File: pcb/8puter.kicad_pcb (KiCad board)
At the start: 2 copper layers, 120 x 100 mm, 82 parts, among them J1 PWR-DC, U2 74AHC74, U3 SN74LVC1G14DBV, U6 MAX811MEUS-T, X1 ECS-2200BX-100, Y1 1.8432MHz

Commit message: Gerber Plots
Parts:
- moved JTAG1 0.20 mm to (184.4, 119.4)
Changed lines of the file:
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@@
   )
   (footprint "Connector_PinHeader_2.00mm:PinHeader_1x05_P2.00mm_Vertical" (layer "F.Cu")
-    (at 184.598 119.445 180)
+    (at 184.398 119.445 180)
     (descr "Through hole straight pin header, 1x05, 2.00mm pitch, single row")
     (tags "Through hole pin header THT 1x05 2.00mm single row")
@@
     (style (thickness 0.1) (arrow_length 1.27) (text_position_mode 0) (extension_height 0.58642) (extension_offset 0.5) keep_text_aligned)
   )
-  (segment (start 186.198 110.545) (end 186.198 112.645) (width 0.2) (layer "F.Cu") (net 1))
   (segment (start 167.898 58.395) (end 167.898 59.597162) (width 0.2) (layer "F.Cu") (net 1))
   (segment (start 105.398 52.245) (end 102.798 52.245) (width 0.5) (layer "F.Cu") (net 1))
   (segment (start 167.798489 60.193327) (end 168.150162 60.545) (width 0.2) (layer "F.Cu") (net 1))
-  (segment (start 185.398 113.445) (end 184.598 113.445) (width 0.2) (layer "F.Cu") (net 1))
   (segment (start 132.298 38.645) (end 125.498 38.645) (width 0.4) (layer "F.Cu") (net 1))
   (segment (start 101.298 53.745) (end 96.198 53.745) (width 0.5) (layer "F.Cu") (net 1))
   (segment (start 169.8105 51.9825) (end 172.49752 51.9825) (width 0.2) (layer "F.Cu") (net 1))
   (segment (start 164.543349 51.9825) (end 169.8105 51.9825) (width 0.2) (layer "F.Cu") (net 1))
+  (segment (start 184.673 109.02) (end 186.198 110.545) (width 0.2) (layer "F.Cu") (net 1))
   (segment (start 167.898 58.395) (end 167.898 55.245) (width 0.2) (layer "F.Cu") (net 1))
   (segment (start 98.063 70.53) (end 103.683 70.53) (width 0.4) (layer "F.Cu") (net 1))
@@
   (segment (start 193.023 54.995) (end 193.023 58.82) (width 0.3) (layer "F.Cu") (net 1))
   (segment (start 188.473 58.52) (end 189.098 59.145) (width 0.3) (layer "F.Cu") (net 1))
-  (segment (start 186.198 112.645) (end 185.398 113.445) (width 0.2) (layer "F.Cu") (net 1))
+  (segment (start 184.673 108.645) (end 184.673 109.02) (width 0.2) (layer "F.Cu") (net 1))
   (segment (start 191.073 54.995) (end 191.073 53.82) (width 0.3) (layer "F.Cu") (net 1))
   (segment (start 188.473 54.995) (end 188.473 58.52) (width 0.3) (layer "F.Cu") (net 1))
@@
   (segment (start 172.49752 51.94548) (end 172.898 51.545) (width 0.2) (layer "F.Cu") (net 1))
   (segment (start 102.798 52.245) (end 102.698 52.345) (width 0.5) (layer "F.Cu") (net 1))
+  (segment (start 186.198 112.645) (end 185.398 113.445) (width 0.2) (layer "F.Cu") (net 1))
   (segment (start 167.898 59.597162) (end 167.798489 59.696673) (width 0.2) (layer "F.Cu") (net 1))
   (segment (start 189.198 59.245) (end 190.348 59.245) (width 0.2) (layer "F.Cu") (net 1))
@@
   (segment (start 106.398 70.545) (end 103.798 70.545) (width 0.4) (layer "F.Cu") (net 1))
   (segment (start 103.798 70.545) (end 103.748 70.595) (width 0.4) (layer "F.Cu") (net 1))
+  (segment (start 186.198 110.545) (end 186.198 112.645) (width 0.2) (layer "F.Cu") (net 1))
   (segment (start 141.998 46.845) (end 142.498 46.345) (width 0.4) (layer "F.Cu") (net 1))
   (segment (start 178.848005 112.307488) (end 178.848005 113.994988) (width 0.2) (layer "F.Cu") (net 1))
-  (segment (start 184.673 109.02) (end 186.198 110.545) (width 0.2) (layer "F.Cu") (net 1))
   (segment (start 167.898 55.245) (end 167.6355 54.9825) (width 0.2) (layer "F.Cu") (net 1))
   (segment (start 141.648 46.845) (end 141.998 46.845) (width 0.4) (layer "F.Cu") (net 1))
@@
   (segment (start 167.798489 59.696673) (end 167.798489 60.193327) (width 0.2) (layer "F.Cu") (net 1))
   (segment (start 103.683 70.53) (end 103.748 70.595) (width 0.4) (layer "F.Cu") (net 1))
-  (segment (start 184.673 108.645) (end 184.673 109.02) (width 0.2) (layer "F.Cu") (net 1))
+  (segment (start 185.398 113.445) (end 184.398 113.445) (width 0.2) (layer "F.Cu") (net 1))
   (via (at 202.898 126.345) (size 0.8) (drill 0.4) (layers "F.Cu" "B.Cu") (net 1))
   (via (at 202.898 124.145) (size 0.8) (drill 0.4) (layers "F.Cu" "B.Cu") (net 1))
@@
   (segment (start 202.898 124.145) (end 197.698 124.145) (width 0.4) (layer "B.Cu") (net 1))
   (segment (start 176.898005 113.944988) (end 179.298005 113.944988) (width 0.4) (layer "B.Cu") (net 1))
-  (segment (start 179.298005 113.944988) (end 184.098012 113.944988) (width 0.4) (layer "B.Cu") (net 1))
   (segment (start 183.028 44.715) (end 196.168 44.715) (width 0.5) (layer "B.Cu") (net 1))
   (segment (start 172.898 52.845) (end 175.098 55.045) (width 0.2) (layer "B.Cu") (net 1))
@@
   (segment (start 136.698 52.945) (end 136.198 53.445) (width 0.25) (layer "B.Cu") (net 1))
   (segment (start 185.598 78.945) (end 191.298 78.945) (width 0.5) (layer "B.Cu") (net 1))
-  (segment (start 184.098012 113.944988) (end 184.598 113.445) (width 0.4) (layer "B.Cu") (net 1))
+  (segment (start 179.298005 113.944988) (end 183.898012 113.944988) (width 0.4) (layer "B.Cu") (net 1))
   (segment (start 172.898 51.545) (end 172.898 52.845) (width 0.2) (layer "B.Cu") (net 1))
   (segment (start 125.598 38.645) (end 125.598 41.345) (width 0.4) (layer "B.Cu") (net 1))
@@
   (segment (start 141.498 41.2945) (end 141.498 38.945) (width 0.4) (layer "B.Cu") (net 1))
   (segment (start 198.198 85.845) (end 198.198 86.345) (width 0.5) (layer "B.Cu") (net 1))
+  (segment (start 183.898012 113.944988) (end 184.398 113.445) (width 0.4) (layer "B.Cu") (net 1))
   (segment (start 130.298 53.445) (end 128.008 51.155) (width 0.25) (layer "B.Cu") (net 1))
   (segment (start 115.598 46.245) (end 118.298 46.245) (width 0.4) (layer "B.Cu") (net 1))
@@
   (segment (start 182.398 130.245) (end 182.373989 130.269011) (width 0.2) (layer "B.Cu") (net 58))
   (segment (start 97.422011 130.269011) (end 95.498 128.345) (width 0.2) (layer "B.Cu") (net 58))
+  (segment (start 179.852219 111.890781) (end 180.298 111.445) (width 0.25) (layer "F.Cu") (net 59))
   (segment (start 179.852219 112.303274) (end 179.852219 111.890781) (width 0.25) (layer "F.Cu") (net 59))
   (segment (start 180.298 111.445) (end 184.598 111.445) (width 0.25) (layer "F.Cu") (net 59))
-  (segment (start 179.852219 111.890781) (end 180.298 111.445) (width 0.25) (layer "F.Cu") (net 59))
   (segment (start 186.198005 71.894988) (end 186.198005 66.945005) (width 0.15) (layer "F.Cu") (net 60))
   (segment (start 186.198 66.345) (end 186.523 66.02) (width 0.15) (layer "F.Cu") (net 60))
@@
   (segment (start 181.398 120.6575) (end 181.3105 120.745) (width 0.2) (layer "F.Cu") (net 74))
   (segment (start 180.539719 115.990774) (end 181.243774 115.990774) (width 0.2) (layer "F.Cu") (net 74))
-  (segment (start 180.539719 114.490774) (end 181.332365 114.490774) (width 0.15) (layer "F.Cu") (net 75))
-  (segment (start 183.098 117.945) (end 184.598 119.445) (width 0.15) (layer "F.Cu") (net 75))
-  (segment (start 183.098 116.256409) (end 183.098 117.945) (width 0.15) (layer "F.Cu") (net 75))
+  (segment (start 183.098 116.256409) (end 183.098 118.145) (width 0.15) (layer "F.Cu") (net 75))
   (segment (start 181.332365 114.490774) (end 183.098 116.256409) (width 0.15) (layer "F.Cu") (net 75))
-  (segment (start 186.898 115.145) (end 184.598 117.445) (width 0.2) (layer "F.Cu") (net 76))
-  (segment (start 186.898 109.045) (end 186.898 115.145) (width 0.2) (layer "F.Cu") (net 76))
-  (segment (start 184.598 117.195) (end 184.598 117.445) (width 0.15) (layer "F.Cu") (net 76))
-  (segment (start 181.393774 113.990774) (end 184.598 117.195) (width 0.15) (layer "F.Cu") (net 76))
-  (segment (start 180.539719 113.990774) (end 181.393774 113.990774) (width 0.15) (layer "F.Cu") (net 76))
+  (segment (start 183.098 118.145) (end 184.398 119.445) (width 0.15) (layer "F.Cu") (net 75))
+  (segment (start 180.539719 114.490774) (end 181.332365 114.490774) (width 0.15) (layer "F.Cu") (net 75))
   (segment (start 186.498 108.645) (end 186.898 109.045) (width 0.2) (layer "F.Cu") (net 76))
-  (segment (start 183.198 114.045) (end 184.598 115.445) (width 0.25) (layer "F.Cu") (net 77))
-  (segment (start 183.198 112.445) (end 183.198 114.045) (width 0.25) (layer "F.Cu") (net 77))
-  (segment (start 182.798 112.045) (end 183.198 112.445) (width 0.25) (layer "F.Cu") (net 77))
+  (segment (start 180.539719 113.990774) (end 181.32666 113.990774) (width 0.15) (layer "F.Cu") (net 76))
+  (segment (start 186.898 114.945) (end 184.398 117.445) (width 0.2) (layer "F.Cu") (net 76))
+  (segment (start 181.32666 113.990774) (end 183.44752 116.111634) (width 0.15) (layer "F.Cu") (net 76))
+  (segment (start 183.698 117.445) (end 184.398 117.445) (width 0.15) (layer "F.Cu") (net 76))
+  (segment (start 186.898 109.045) (end 186.898 114.945) (width 0.2) (layer "F.Cu") (net 76))
+  (segment (start 183.44752 116.111634) (end 183.44752 117.19452) (width 0.15) (layer "F.Cu") (net 76))
+  (segment (start 183.44752 117.19452) (end 183.698 117.445) (width 0.15) (layer "F.Cu") (net 76))
   (segment (start 180.539719 112.303281) (end 180.798 112.045) (width 0.25) (layer "F.Cu") (net 77))
+  (segment (start 182.798 112.045) (end 183.198 112.445) (width 0.25) (layer "F.Cu") (net 77))
   (segment (start 180.539719 112.990774) (end 180.539719 112.303281) (width 0.25) (layer "F.Cu") (net 77))
+  (segment (start 183.198 112.445) (end 183.198 114.245) (width 0.25) (layer "F.Cu") (net 77))
   (segment (start 180.798 112.045) (end 182.798 112.045) (width 0.25) (layer "F.Cu") (net 77))
+  (segment (start 183.198 114.245) (end 184.398 115.445) (width 0.25) (layer "F.Cu") (net 77))
   (segment (start 143.198 51.245) (end 143.198 53.3075) (width 0.25) (layer "F.Cu") (net 89))
   (segment (start 143.198 53.3075) (end 143.1605 53.345) (width 0.25) (layer "F.Cu") (net 89))

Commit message: board improvements
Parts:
- moved D1 0.05 mm to (100.3, 51.4), turned to -90 degrees
- turned U3 to -90 degrees
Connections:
- CS_SEL1 pad 5: GND -> unconnected-(CS_SEL1-Pad5)
- DEBUG1 pad 30: RDY -> ~{IRQ}
- DEBUG1 pad 32: CLOCK -> RDY
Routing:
- net ~{IRQ}: track 70.3 -> 190.2 mm
- net CLOCK: track 276.9 -> 157.8 mm
- net +5V: track 250.0 -> 187.8 mm, vias 5 -> 6
- net GND: track 253.9 -> 225.0 mm, vias 28 -> 26
- net ADDR0: track 178.5 -> 168.7 mm
- net ADDR1: track 184.7 -> 176.3 mm
- net RDY: track 189.7 -> 185.4 mm
- net Net-(C18-Pad1): track 7.55 -> 10.9 mm
- net Net-(U2-Pad12): track 7.45 -> 9.47 mm
- net Net-(U2-Pad11): track 8.96 -> 7.68 mm
- net Net-(C13-Pad1): track 52.2 -> 53.4 mm
- net Net-(SERC1-Pad4): track 25.3 -> 24.2 mm
- net /Peripheral Handler/PC1: track 53.1 -> 53.9 mm
- net /Power/PWR: track 23.4 -> 24.0 mm
- net Net-(D1-Pad1): track 3.16 -> 2.60 mm
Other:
- board text added: "~{IRQ}"
- board text removed: "CLK"

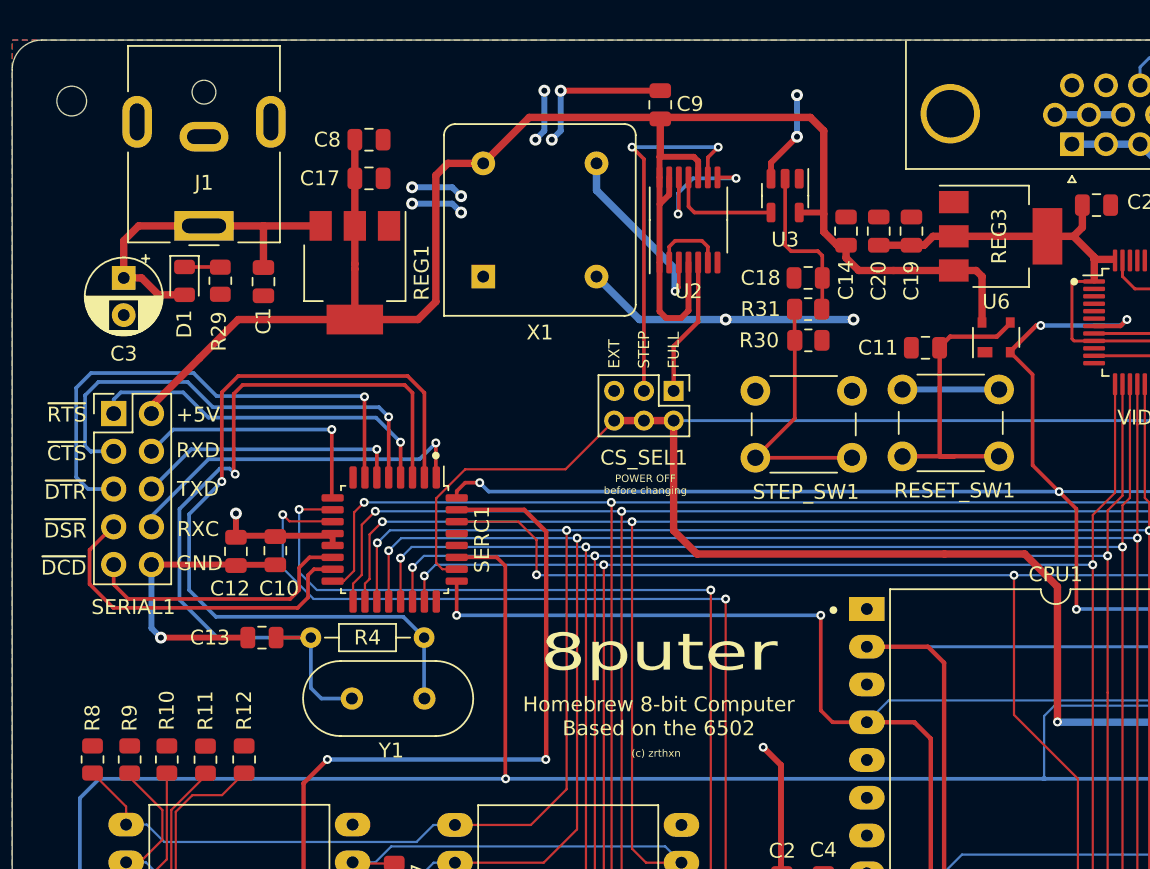
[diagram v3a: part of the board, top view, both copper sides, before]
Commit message: update schematic
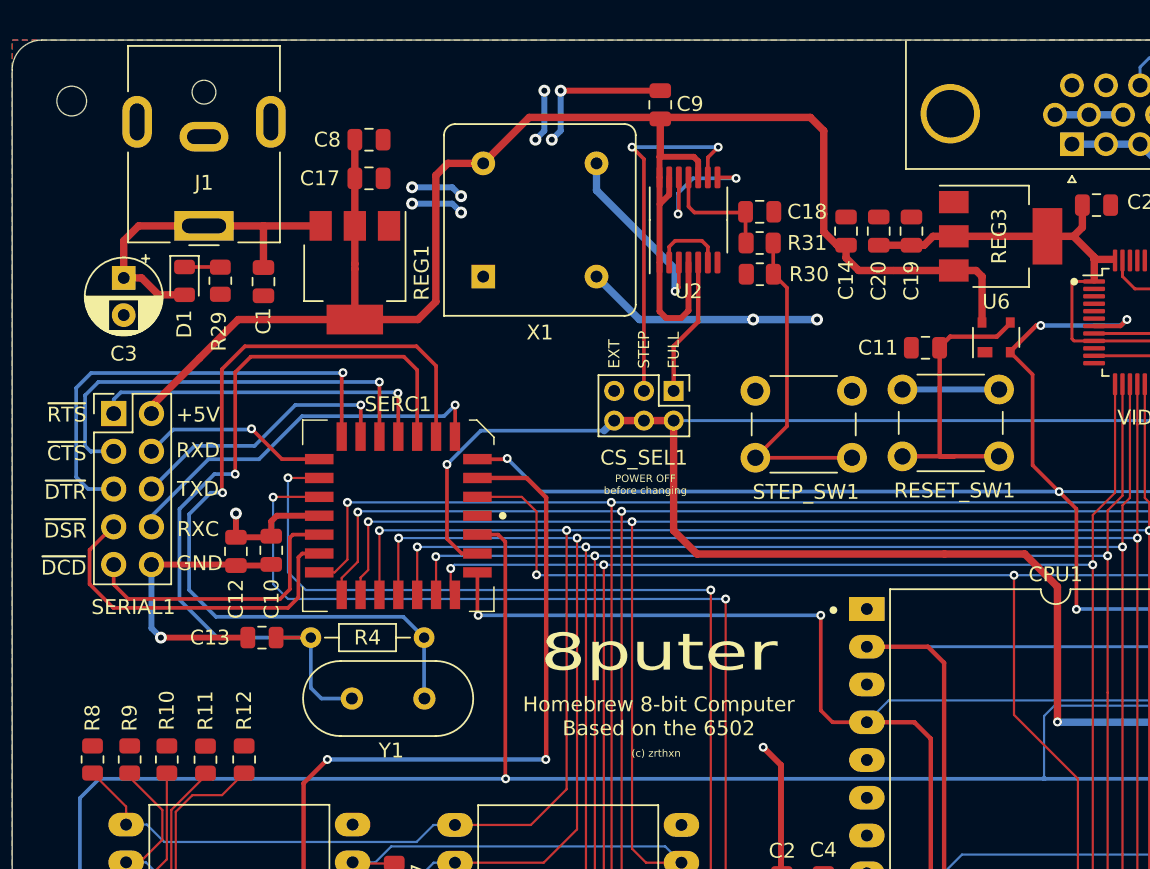
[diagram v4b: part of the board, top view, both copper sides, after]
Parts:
- removed U3: SN74LVC1G14DBV, Package_TO_SOT_SMD:SOT-23-5
- SERC1: value W65C51NxQ -> W65C51NxPL; footprint Package_QFP:LQFP-32_7x7mm_P0.8mm -> Package_LCC:PLCC-28
- U6: value MAX811MEUS-T -> MAX811TEUS+T
- moved R30 5.52 mm to (139.0, 51.0), turned to 0 degrees
- moved C18 5.52 mm to (139.0, 46.8), turned to 0 degrees
- moved R31 5.52 mm to (139.0, 48.9), turned to 180 degrees
- moved SERC1 1.62 mm to (114.7, 67.2)
- moved C10 0.28 mm to (106.1, 69.6)
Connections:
- C13 pad 1: Net-(C13-Pad1) -> Net-(Y1-Pad1)
- R4 pad 1: Net-(R4-Pad1) -> Net-(Y1-Pad2)
- R4 pad 2: Net-(C13-Pad1) -> Net-(Y1-Pad1)
- SERC1 pad 1: Net-(SERC1-Pad1) -> GND
- SERC1 pad 10: ADDR0 -> Net-(SERC1-Pad10)
- SERC1 pad 11: ADDR1 -> Net-(SERIAL1-Pad5)
- SERC1 pad 12: +5V -> Net-(SERC1-Pad12)
- SERC1 pad 13: +5V -> ADDR0
- SERC1 pad 14: Net-(SERC1-Pad14) -> ADDR1
- SERC1 pad 15: Net-(SERC1-Pad15) -> +5V
- SERC1 pad 16: DATA0 -> Net-(SERIAL1-Pad9)
- SERC1 pad 17: DATA1 -> Net-(SERIAL1-Pad7)
- SERC1 pad 18: DATA2 -> DATA0
- SERC1 pad 19: DATA3 -> DATA1
- SERC1 pad 2: Net-(R4-Pad1) -> ADDR15
- SERC1 pad 20: DATA4 -> DATA2
- SERC1 pad 21: DATA5 -> DATA3
- SERC1 pad 22: DATA6 -> DATA4
- SERC1 pad 23: DATA7 -> DATA5
- SERC1 pad 24: unconnected-(SERC1-Pad24) -> DATA6
- SERC1 pad 25: ~{IRQ} -> DATA7
- SERC1 pad 26: CLOCK -> ~{IRQ}
- SERC1 pad 27: CPU_R~{W} -> CLOCK
- SERC1 pad 28: GND -> CPU_R~{W}
- SERC1 pad 3: Net-(C13-Pad1) -> ~{SERIAL_CS}
- SERC1 pad 4: Net-(SERC1-Pad4) -> ~{RESET}
- SERC1 pad 6: Net-(SERC1-Pad6) -> Net-(Y1-Pad2)
- SERC1 pad 7: Net-(SERC1-Pad7) -> Net-(Y1-Pad1)
- SERC1 pad 8: unconnected-(SERC1-Pad8) -> Net-(SERIAL1-Pad1)
- SERC1 pad 9: Net-(SERC1-Pad9) -> Net-(SERIAL1-Pad3)
- SERIAL1 pad 1: Net-(SERC1-Pad4) -> Net-(SERIAL1-Pad1)
- SERIAL1 pad 3: Net-(SERC1-Pad5) -> Net-(SERIAL1-Pad3)
- SERIAL1 pad 4: Net-(SERC1-Pad9) -> Net-(SERC1-Pad12)
- SERIAL1 pad 5: Net-(SERC1-Pad7) -> Net-(SERIAL1-Pad5)
- SERIAL1 pad 6: Net-(SERC1-Pad6) -> Net-(SERC1-Pad10)
- SERIAL1 pad 7: Net-(SERC1-Pad15) -> Net-(SERIAL1-Pad7)
- SERIAL1 pad 8: Net-(SERC1-Pad1) -> Net-(SERC1-Pad5)
- SERIAL1 pad 9: Net-(SERC1-Pad14) -> Net-(SERIAL1-Pad9)
- U2 pad 11: Net-(U2-Pad11) -> Net-(C18-Pad1)
- Y1 pad 1: Net-(C13-Pad1) -> Net-(Y1-Pad1)
- Y1 pad 2: Net-(R4-Pad1) -> Net-(Y1-Pad2)
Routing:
- net Net-(Y1-Pad2): track 0.00 -> 57.9 mm, vias 0 -> 1
- net Net-(R4-Pad1): track 55.7 -> 0.00 mm, vias 1 -> 0
- net Net-(Y1-Pad1): track 0.00 -> 53.9 mm, vias 0 -> 1
- net Net-(C13-Pad1): track 53.4 -> 0.00 mm, vias 1 -> 0
- net Net-(SERC1-Pad7): track 34.8 -> 0.00 mm, vias 1 -> 0
- net Net-(SERIAL1-Pad5): track 0.00 -> 31.6 mm, vias 0 -> 1
- net Net-(SERIAL1-Pad3): track 0.00 -> 29.4 mm, vias 0 -> 1
- net Net-(SERC1-Pad1): track 24.2 -> 0.00 mm, vias 1 -> 0
- net Net-(SERC1-Pad4): track 24.2 -> 0.00 mm, vias 1 -> 0
- net Net-(SERIAL1-Pad7): track 0.00 -> 23.8 mm
- net Net-(SERC1-Pad15): track 23.5 -> 0.00 mm
- net Net-(SERIAL1-Pad1): track 0.00 -> 23.2 mm, vias 0 -> 1
- net Net-(SERIAL1-Pad9): track 0.00 -> 19.4 mm
- net Net-(SERC1-Pad10): track 0.00 -> 18.6 mm, vias 0 -> 1
- net Net-(SERC1-Pad14): track 18.5 -> 0.00 mm
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
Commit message: serial rollback
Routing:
- net CLOCK: track 157.7 -> 134.9 mm, vias 4 -> 5
- net CPU_R~{W}: track 189.6 -> 198.6 mm
- net ADDR15: track 190.4 -> 194.5 mm
- net ~{RESET}: track 145.8 -> 146.7 mm
